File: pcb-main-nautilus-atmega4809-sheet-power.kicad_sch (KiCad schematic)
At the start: 14 parts, among them U1 NCP1117-5.0_TO252, U2 AP2112K-3.3

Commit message: Update BOM
Supports #2.
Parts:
- C2: Manufacturer Part Number EEE-HC1E470XP -> EEEHC1E470XP
- C4: Manufacturer Part Number EEE-FN1A470UR -> EEEFN1A470UR
- D2, D3: Manufacturer Part Number MBR120LSFT3G -> MBR120LSF
- R2, R3: Manufacturer Part Number ERJ-3EKF3300V -> ERJ-3EKF3300
- U1: Manufacturer Part Number NCP1117DT50RKG -> NCP1117DT50
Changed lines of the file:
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@@
       (effects (font (size 1.27 1.27)) hide)
     )
-    (property "Manufacturer Part Number" "ERJ-3EKF3300V" (id 5) (at 147.32 111.76 0)
+    (property "Manufacturer Part Number" "ERJ-3EKF3300" (id 5) (at 147.32 111.76 0)
       (effects (font (size 1.27 1.27)) hide)
     )
@@
       (effects (font (size 1.27 1.27)) hide)
     )
-    (property "Manufacturer Part Number" "NCP1117DT50RKG" (id 5) (at 101.6 96.52 0)
+    (property "Manufacturer Part Number" "NCP1117DT50" (id 5) (at 101.6 96.52 0)
       (effects (font (size 1.27 1.27)) hide)
     )
@@
       (effects (font (size 1.27 1.27)) hide)
     )
-    (property "Manufacturer Part Number" "EEE-HC1E470XP" (id 5) (at 66.04 101.6 0)
+    (property "Manufacturer Part Number" "EEEHC1E470XP" (id 5) (at 66.04 101.6 0)
       (effects (font (size 1.27 1.27)) hide)
     )
@@
       (effects (font (size 1.27 1.27)) hide)
     )
-    (property "Manufacturer Part Number" "MBR120LSFT3G" (id 5) (at 66.04 91.44 0)
+    (property "Manufacturer Part Number" "MBR120LSF" (id 5) (at 66.04 91.44 0)
       (effects (font (size 1.27 1.27)) hide)
     )
@@
       (effects (font (size 1.27 1.27)) hide)
     )
-    (property "Manufacturer Part Number" "EEE-FN1A470UR" (id 5) (at 116.84 101.6 0)
+    (property "Manufacturer Part Number" "EEEFN1A470UR" (id 5) (at 116.84 101.6 0)
       (effects (font (size 1.27 1.27)) hide)
     )
@@
       (effects (font (size 1.27 1.27)) hide)
     )
-    (property "Manufacturer Part Number" "MBR120LSFT3G" (id 5) (at 116.84 91.44 0)
+    (property "Manufacturer Part Number" "MBR120LSF" (id 5) (at 116.84 91.44 0)
       (effects (font (size 1.27 1.27)) hide)
     )
@@
       (effects (font (size 1.27 1.27)) hide)
     )
-    (property "Manufacturer Part Number" "ERJ-3EKF3300V" (id 5) (at 213.36 111.76 0)
-      (effects (font (size 1.27 1.27)) hide)
-    )
+    (property "Manufacturer Part Number" "ERJ-3EKF3300" (id 5) (at 213.36 111.76 0)
+      (effects (font (size 1.27 1.27)) hide)
+    )

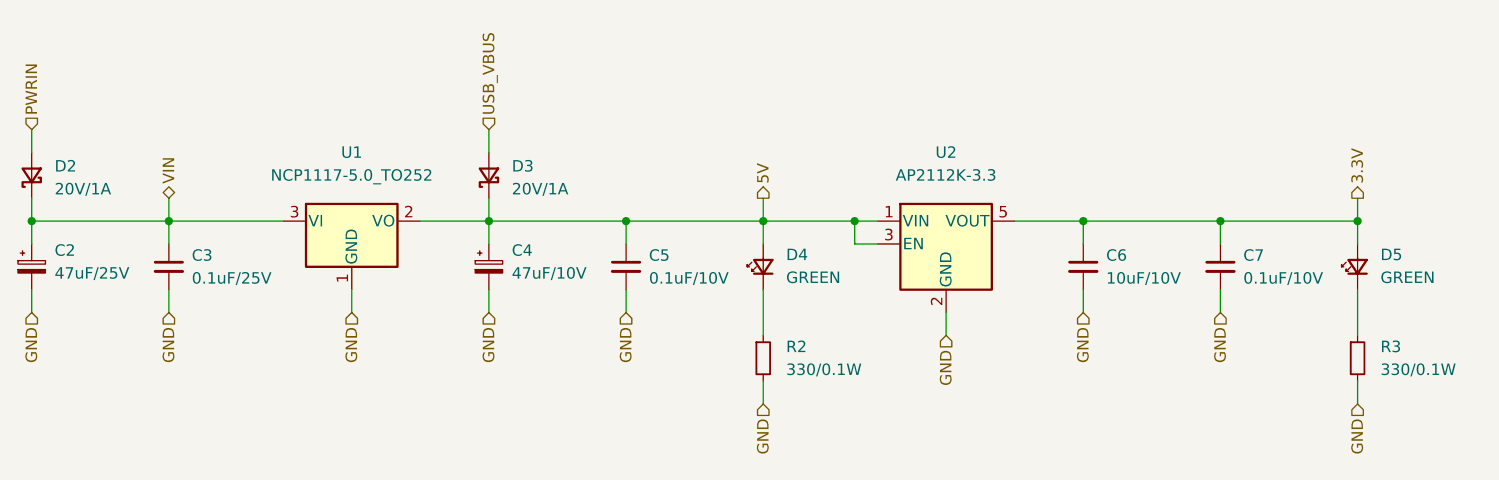
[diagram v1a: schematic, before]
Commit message: Add test points
Supports #2.
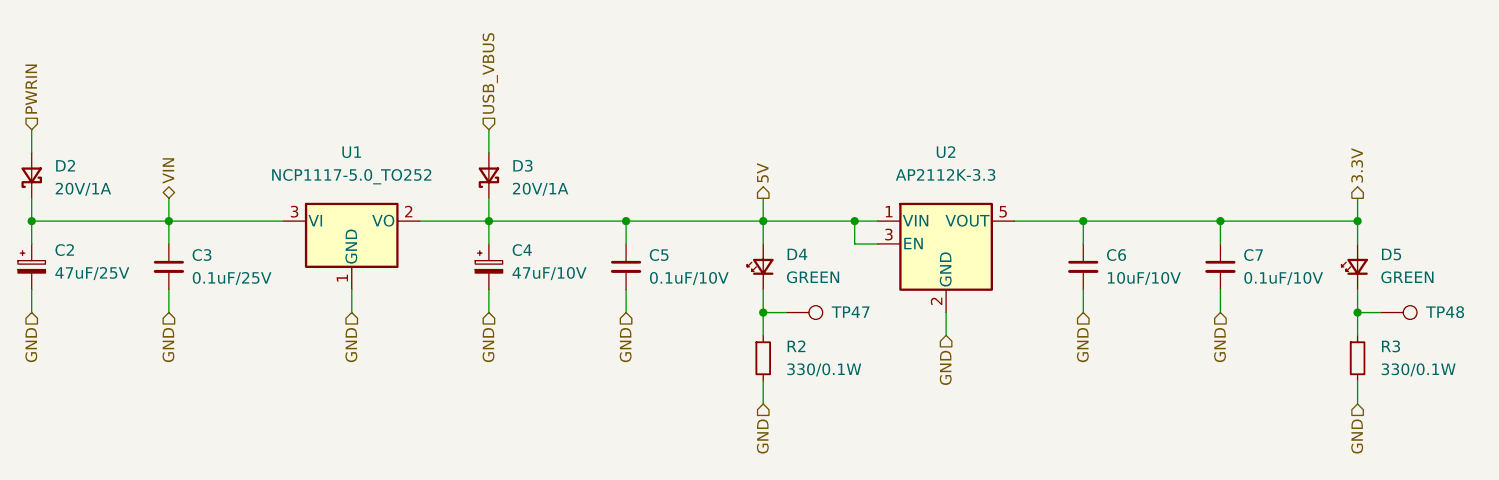
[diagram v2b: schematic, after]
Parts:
- added TP47, TP48: TestPoint, TestPoint:TestPoint_Pad_D1.0mm, symbol Connector:TestPoint
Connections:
- net at D4.1 (K), R2.1: now also TP47.1
- net at D5.1 (K), R3.1: now also TP48.1
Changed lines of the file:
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@@
   (junction (at 132.08 96.52) (diameter 0) (color 0 0 0 0)
   )
+  (junction (at 147.32 106.68) (diameter 0) (color 0 0 0 0)
+  )
+  (junction (at 213.36 106.68) (diameter 0) (color 0 0 0 0)
+  )
   (junction (at 66.04 96.52) (diameter 0) (color 0 0 0 0)
   )
@@
     (stroke (width 0) (type default) (color 0 0 0 0))
   )
-  (wire (pts (xy 147.32 104.14) (xy 147.32 109.22))
+  (wire (pts (xy 147.32 106.68) (xy 147.32 109.22))
+    (stroke (width 0) (type default) (color 0 0 0 0))
+  )
+  (wire (pts (xy 147.32 104.14) (xy 147.32 106.68))
     (stroke (width 0) (type default) (color 0 0 0 0))
   )
@@
     (stroke (width 0) (type default) (color 0 0 0 0))
   )
+  (wire (pts (xy 213.36 106.68) (xy 215.9 106.68))
+    (stroke (width 0) (type default) (color 0 0 0 0))
+  )
+  (wire (pts (xy 147.32 106.68) (xy 149.86 106.68))
+    (stroke (width 0) (type default) (color 0 0 0 0))
+  )
   (wire (pts (xy 66.04 86.36) (xy 66.04 88.9))
     (stroke (width 0) (type default) (color 0 0 0 0))
@@
     (stroke (width 0) (type default) (color 0 0 0 0))
   )
-  (wire (pts (xy 213.36 104.14) (xy 213.36 109.22))
+  (wire (pts (xy 213.36 104.14) (xy 213.36 106.68))
     (stroke (width 0) (type default) (color 0 0 0 0))
   )
@@
   )
   (wire (pts (xy 147.32 114.3) (xy 147.32 116.84))
+    (stroke (width 0) (type default) (color 0 0 0 0))
+  )
+  (wire (pts (xy 213.36 106.68) (xy 213.36 109.22))
     (stroke (width 0) (type default) (color 0 0 0 0))
   )
@@
     (pin "3")
   )
+  (symbol (lib_id "Connector:TestPoint") (at 215.9 106.68 270) (unit 1)
+    (in_bom yes) (on_board yes)
+    (property "Reference" "TP48" (id 0) (at 220.98 106.68 90)
+      (effects (font (size 1.27 1.27)) (justify left))
+    )
+    (property "Value" "TestPoint" (id 1) (at 217.9321 109.22 0)
+      (effects (font (size 1.27 1.27)) (justify left) hide)
+    )
+    (property "Footprint" "TestPoint:TestPoint_Pad_D1.0mm" (id 2) (at 215.9 111.76 0)
+      (effects (font (size 1.27 1.27)) hide)
+    )
+    (property "Datasheet" "~" (id 3) (at 215.9 111.76 0)
+      (effects (font (size 1.27 1.27)) hide)
+    )
+    (pin "1")
+  )
   (symbol (lib_id "Device:C_Polarized_Small") (at 66.04 101.6 0) (unit 1)
     (in_bom yes) (on_board yes) (fields_autoplaced)
@@
     (pin "2")
   )
+  (symbol (lib_id "Connector:TestPoint") (at 149.86 106.68 270) (unit 1)
+    (in_bom yes) (on_board yes)
+    (property "Reference" "TP47" (id 0) (at 154.94 106.68 90)
+      (effects (font (size 1.27 1.27)) (justify left))
+    )
+    (property "Value" "TestPoint" (id 1) (at 151.8921 109.22 0)
+      (effects (font (size 1.27 1.27)) (justify left) hide)
+    )
+    (property "Footprint" "TestPoint:TestPoint_Pad_D1.0mm" (id 2) (at 149.86 111.76 0)
+      (effects (font (size 1.27 1.27)) hide)
+    )
+    (property "Datasheet" "~" (id 3) (at 149.86 111.76 0)
+      (effects (font (size 1.27 1.27)) hide)
+    )
+    (pin "1")
+  )
   (symbol (lib_id "Device:C_Small") (at 81.28 101.6 0) (unit 1)

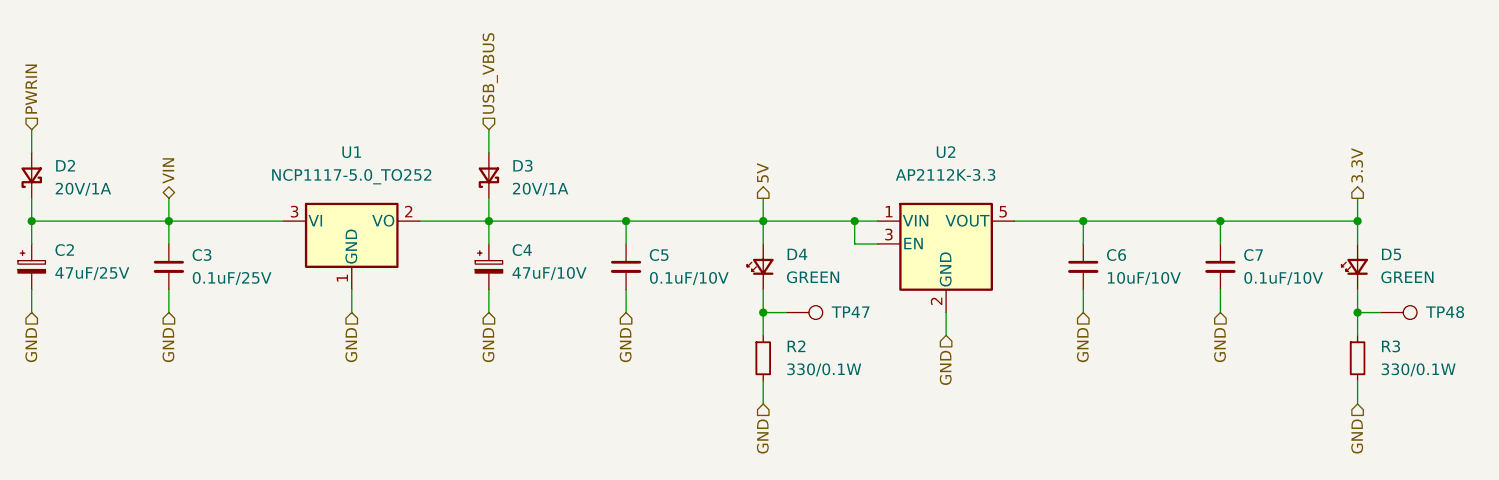
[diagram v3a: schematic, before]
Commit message: Add layout (#4)
Resolves #3 (Add layout).
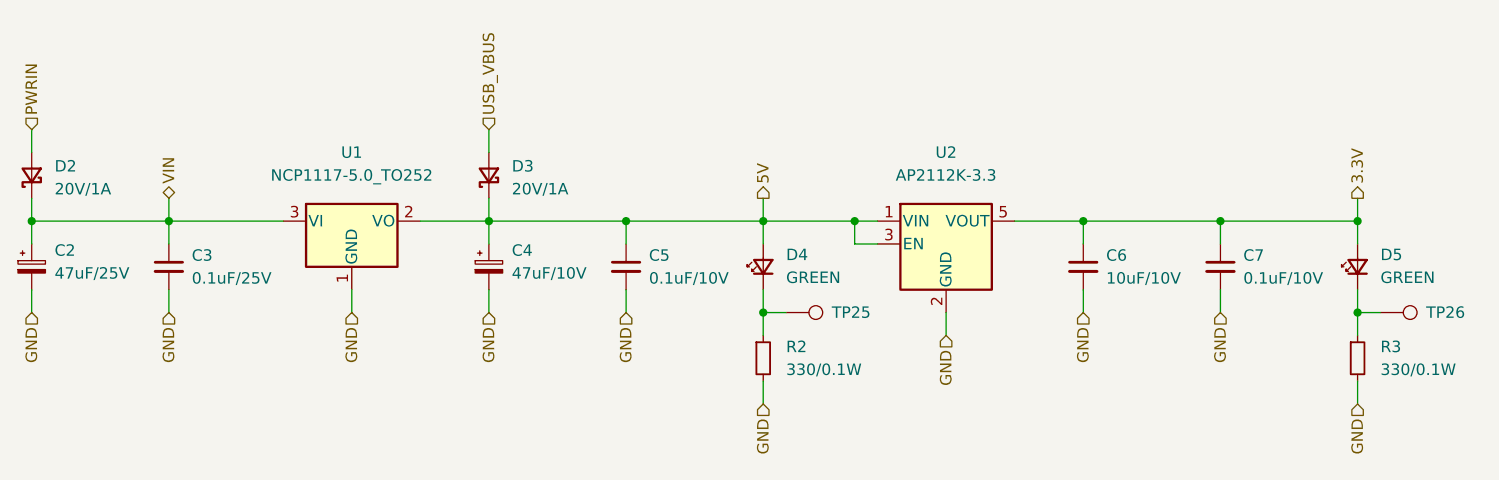
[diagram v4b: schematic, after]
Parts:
- renumbered TP47 to TP25, TP48 to TP26
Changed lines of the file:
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@@
   (symbol (lib_id "Connector:TestPoint") (at 215.9 106.68 270) (unit 1)
     (in_bom yes) (on_board yes)
-    (property "Reference" "TP48" (id 0) (at 220.98 106.68 90)
+    (property "Reference" "TP26" (id 0) (at 220.98 106.68 90)
       (effects (font (size 1.27 1.27)) (justify left))
     )
@@
   (symbol (lib_id "Connector:TestPoint") (at 149.86 106.68 270) (unit 1)
     (in_bom yes) (on_board yes)
-    (property "Reference" "TP47" (id 0) (at 154.94 106.68 90)
+    (property "Reference" "TP25" (id 0) (at 154.94 106.68 90)
       (effects (font (size 1.27 1.27)) (justify left))
     )
